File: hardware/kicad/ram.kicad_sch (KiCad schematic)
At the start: 8 parts, among them U1 LFE5U-25F-6BG381C, U2 MT48LC16M16A2TG, Y1 FNETHE025

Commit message: Updated Rev. 1.1
- Wired Level Shifters
- Expansion GPIOs
- Oscillator
- Flash
- USB
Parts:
- removed U1: LFE5U-25F-6BG381C, lfe5bg381:BGA-381_pitch0.8mm_dia0.4mm, symbol lfe5bg381:LFE5UM-85F-6BG381C
- removed Y1: FNETHE025, oscxo:Crystal_SMD_7050_4Pads, symbol Device:Crystal_GND24
- added U1: LFE5U-25F-6BG381C, lfe5bg381:BGA-381_pitch0.8mm_dia0.4mm, symbol lfe5bg381:LFE5UM-85F-6BG381C

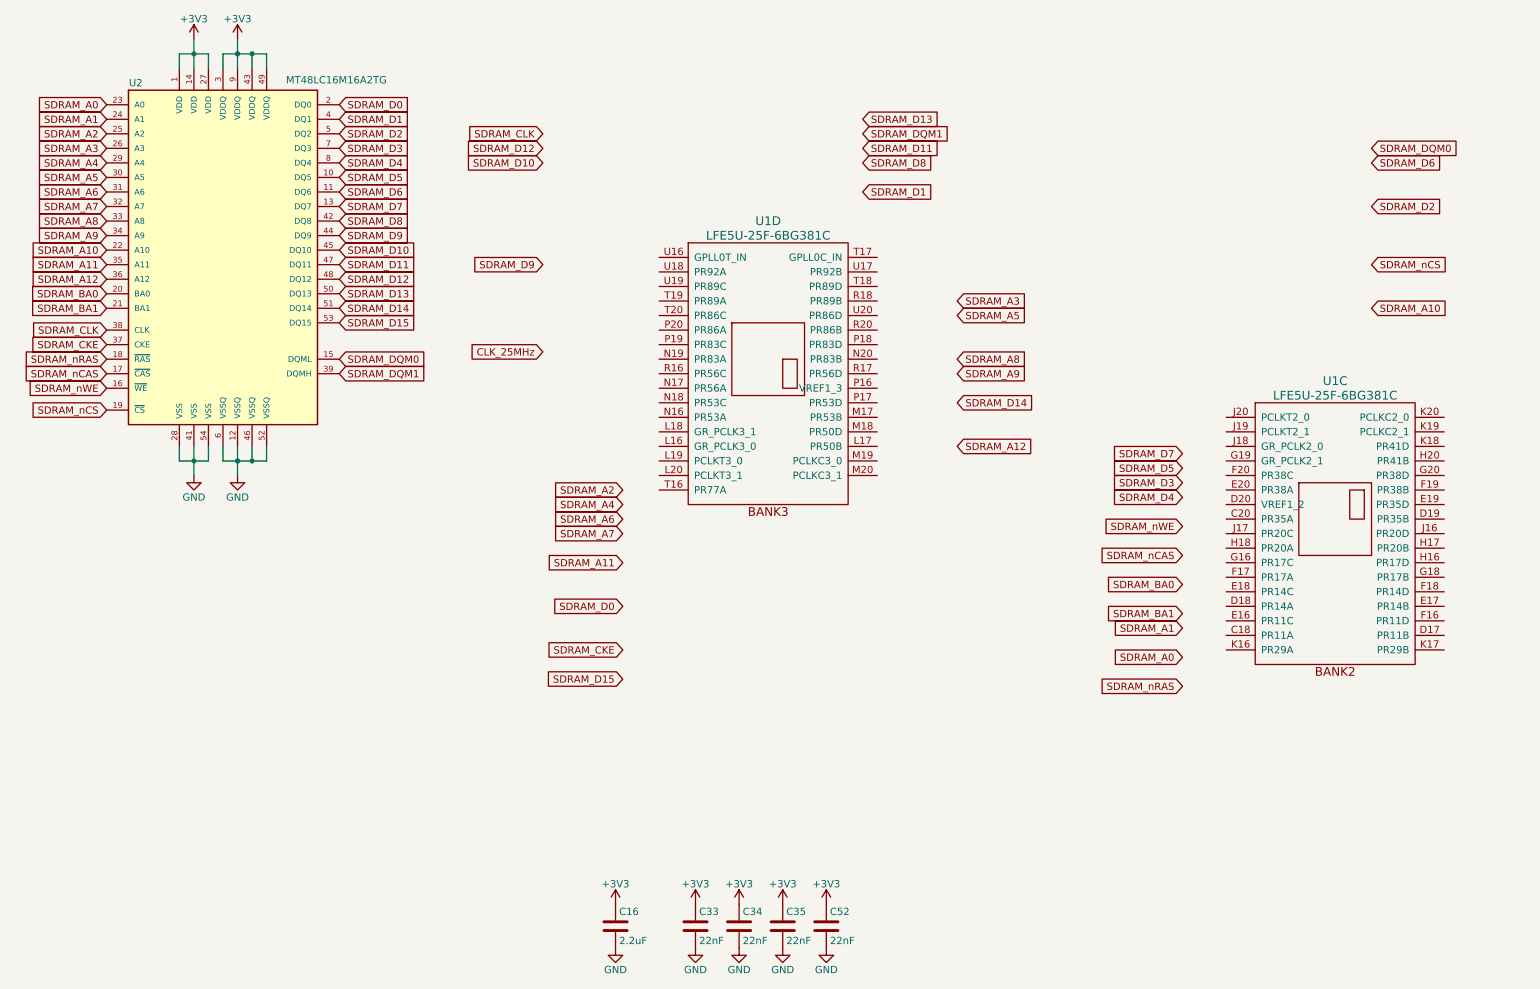
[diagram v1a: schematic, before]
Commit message: Rev. 1.1
Final Revision - DRC passes
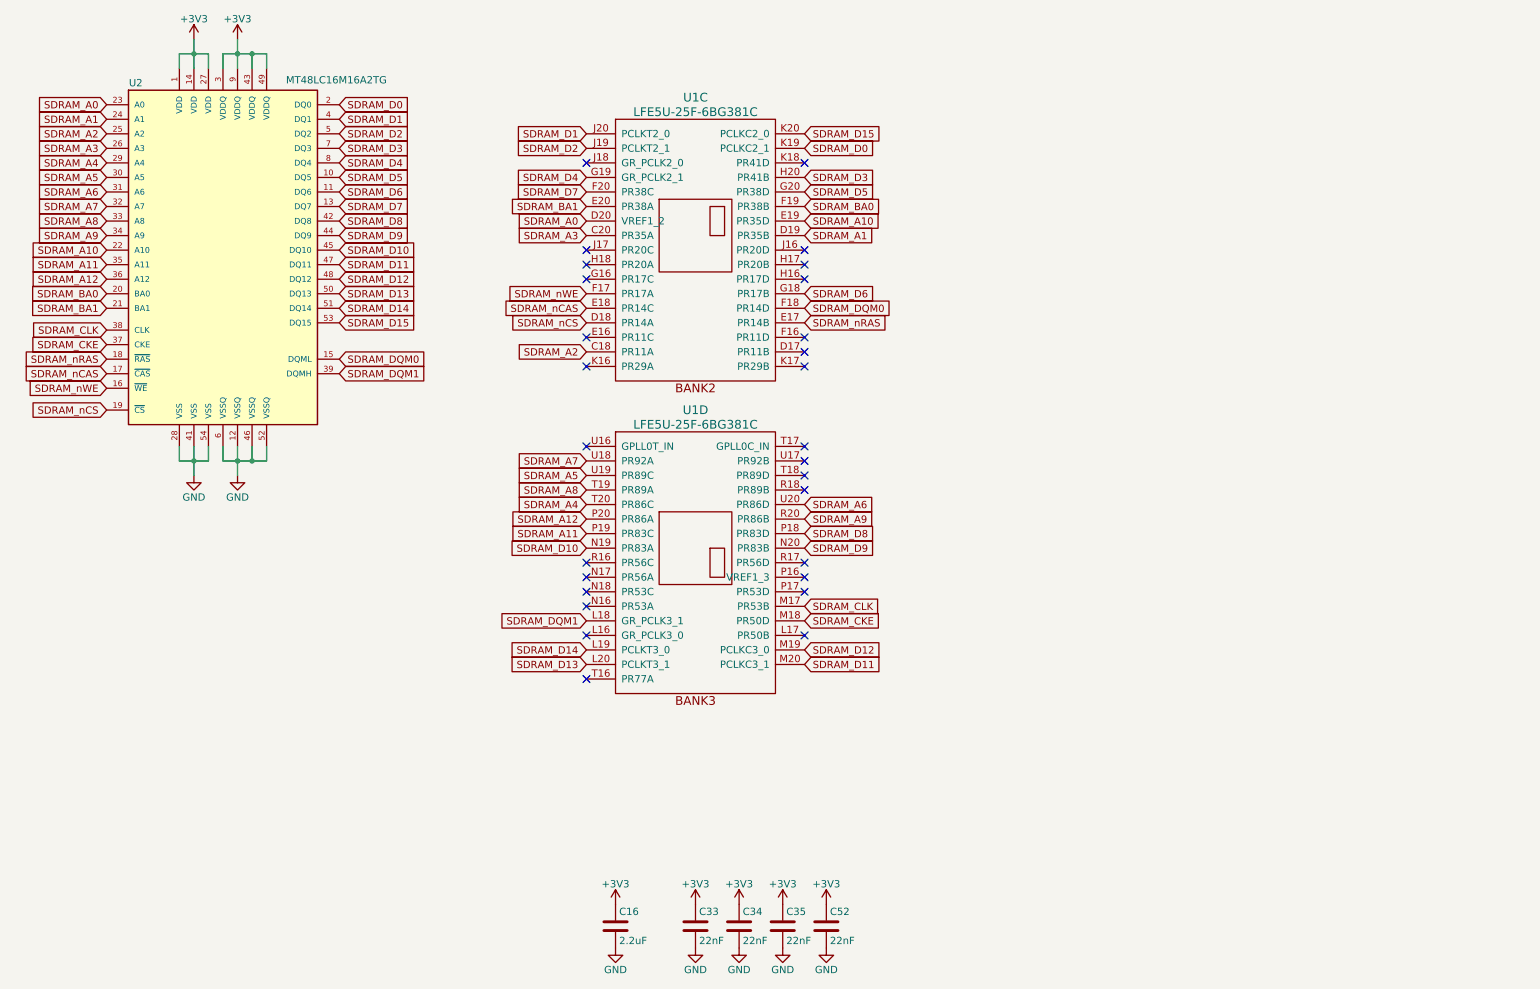
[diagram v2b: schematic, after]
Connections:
- net SDRAM_A0: now also U1.D20 (VREF1_2)
- net SDRAM_A1: now also U1.D19 (PR35B)
- net SDRAM_A10: now also U1.E19 (PR35D)
- net SDRAM_A11: now also U1.P19 (PR83C)
- net SDRAM_A12: now also U1.P20 (PR86A)
- net SDRAM_A2: now also U1.C18 (PR11A)
- net SDRAM_A3: now also U1.C20 (PR35A)
- net SDRAM_A4: now also U1.T20 (PR86C)
- net SDRAM_A5: now also U1.U19 (PR89C)
- net SDRAM_A6: now also U1.U20 (PR86D)
- net SDRAM_A7: now also U1.U18 (PR92A)
- net SDRAM_A8: now also U1.T19 (PR89A)
- net SDRAM_A9: now also U1.R20 (PR86B)
- net SDRAM_BA0: now also U1.F19 (PR38B)
- net SDRAM_BA1: now also U1.E20 (PR38A)
- net SDRAM_CKE: now also U1.M18 (PR50D)
- net SDRAM_CLK: now also U1.M17 (PR53B)
- net SDRAM_D0: now also U1.K19 (PCLKC2_1)
- net SDRAM_D1: now also U1.J20 (PCLKT2_0)
- net SDRAM_D10: now also U1.N19 (PR83A)
- net SDRAM_D11: now also U1.M20 (PCLKC3_1)
- net SDRAM_D12: now also U1.M19 (PCLKC3_0)
- net SDRAM_D13: now also U1.L20 (PCLKT3_1)
- net SDRAM_D14: now also U1.L19 (PCLKT3_0)
- net SDRAM_D15: now also U1.K20 (PCLKC2_0)
- net SDRAM_D2: now also U1.J19 (PCLKT2_1)
- net SDRAM_D3: now also U1.H20 (PR41B)
- net SDRAM_D4: now also U1.G19 (GR_PCLK2_1)
- net SDRAM_D5: now also U1.G20 (PR38D)
- net SDRAM_D6: now also U1.G18 (PR17B)
- net SDRAM_D7: now also U1.F20 (PR38C)
- net SDRAM_D8: now also U1.P18 (PR83D)
- net SDRAM_D9: now also U1.N20 (PR83B)
- net SDRAM_DQM0: now also U1.F18 (PR14D)
- net SDRAM_DQM1: now also U1.L18 (GR_PCLK3_1)
- net SDRAM_nCAS: now also U1.E18 (PR14C)
- net SDRAM_nCS: now also U1.D18 (PR14A)
- net SDRAM_nRAS: now also U1.E17 (PR14B)
- net SDRAM_nWE: now also U1.F17 (PR17A)
- no-connect marks 0 -> 28
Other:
- moved on the sheet: U1C, U1D

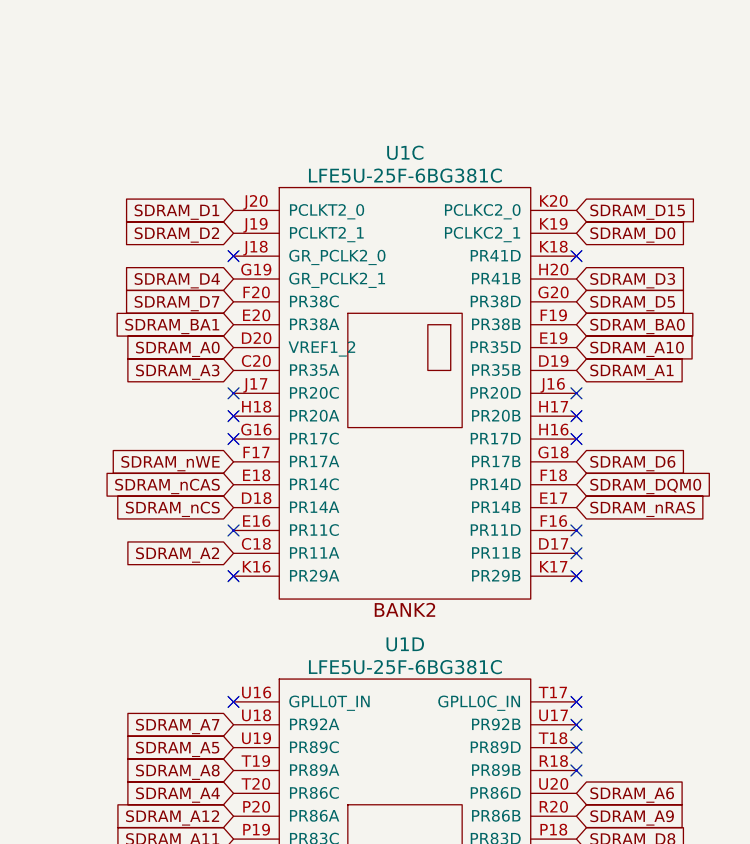
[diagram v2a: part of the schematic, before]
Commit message: Updates FPGA model in BOM and schematics
Replaces LFE5U-25F-6BG381C with LFE5U-85F-8BG381I in multiple files.
Ensures consistency across BOM, schematics, and PCB layouts for the updated FPGA model.
Adjusts related properties such as part number and connectivity attributes.

Addresses a hardware specification upgrade in branch 1.1.
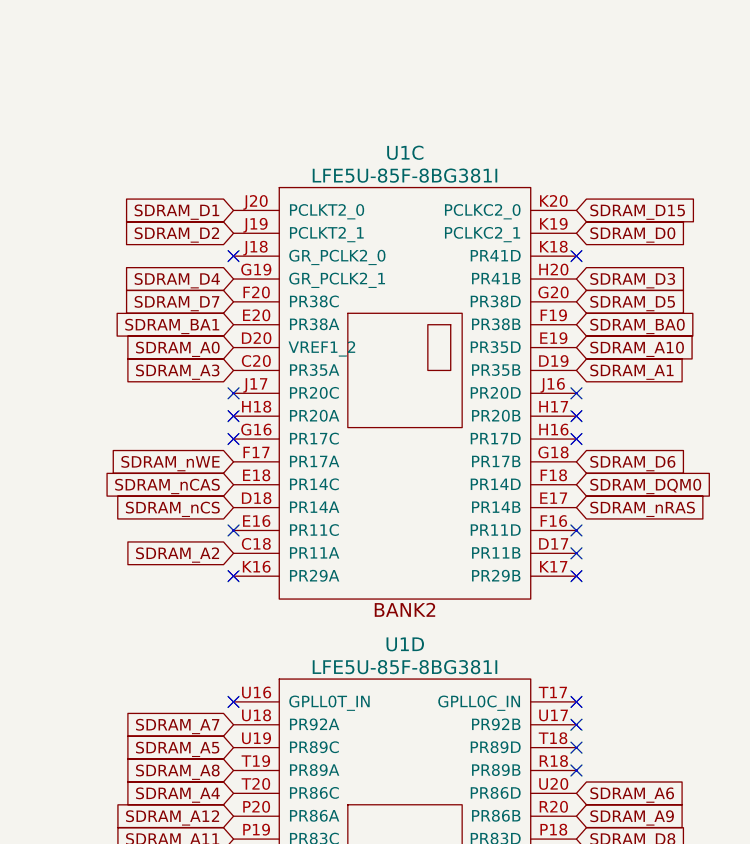
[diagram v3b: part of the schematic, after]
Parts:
- U1: value LFE5U-25F-6BG381C -> LFE5U-85F-8BG381I; MPN LFE5U-85F-6BG381C -> LFE5U-85F-8BG381I
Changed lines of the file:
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@@
 			)
 		)
-		(property "Value" "LFE5U-25F-6BG381C"
+		(property "Value" "LFE5U-85F-8BG381I"
 			(at 139.7 36.83 0)
 			(effects
@@
 			)
 		)
-		(property "MPN" "LFE5U-85F-6BG381C"
+		(property "MPN" "LFE5U-85F-8BG381I"
 			(at 139.7 58.42 0)
 			(effects
@@
 			)
 		)
-		(property "Value" "LFE5U-25F-6BG381C"
+		(property "Value" "LFE5U-85F-8BG381I"
 			(at 139.7 91.44 0)
 			(effects
@@
 			)
 		)
-		(property "MPN" "LFE5U-85F-6BG381C"
+		(property "MPN" "LFE5U-85F-8BG381I"
 			(at 139.7 113.03 0)
 			(effects
